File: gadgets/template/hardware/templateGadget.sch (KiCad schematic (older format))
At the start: 1 part

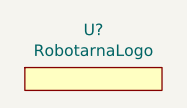
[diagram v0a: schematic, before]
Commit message: Rename smdChallenge to solderingChallenge
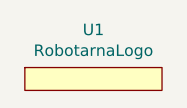
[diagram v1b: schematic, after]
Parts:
- gave numbers to parts that had none: 1
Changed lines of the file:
@@
 $EndDescr
 $Comp
-L RoboCamp:RobotarnaLogo U?
+L RoboCamp:RobotarnaLogo U1
 U 1 1 5FD68B7F
 P 10200 6200
-F 0 "U?" H 10200 6415 50  0000 C CNN
+F 0 "U1" H 10200 6415 50  0000 C CNN
 F 1 "RobotarnaLogo" H 10200 6324 50  0000 C CNN
 F 2 "RoboCamp:RobotarnaLogo-6mm" H 10200 6200 50  0001 C CNN
